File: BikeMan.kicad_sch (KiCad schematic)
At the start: 24 parts, among them J1 USB_A_stacked, J10 Conn_01x06_Male, J11 Conn_01x06_Male, J2 USB_A_stacked, J3 Barrel_Jack, J4 Conn_01x06_Female, J5 Conn_01x06_Female, J6 Conn_01x06_Female, J7 PushConnector_8pos, J8 PushConnector_8pos, J9 PushConnector_8pos, Q1 DMN62D0U-7, Q2 DMN62D0U-7

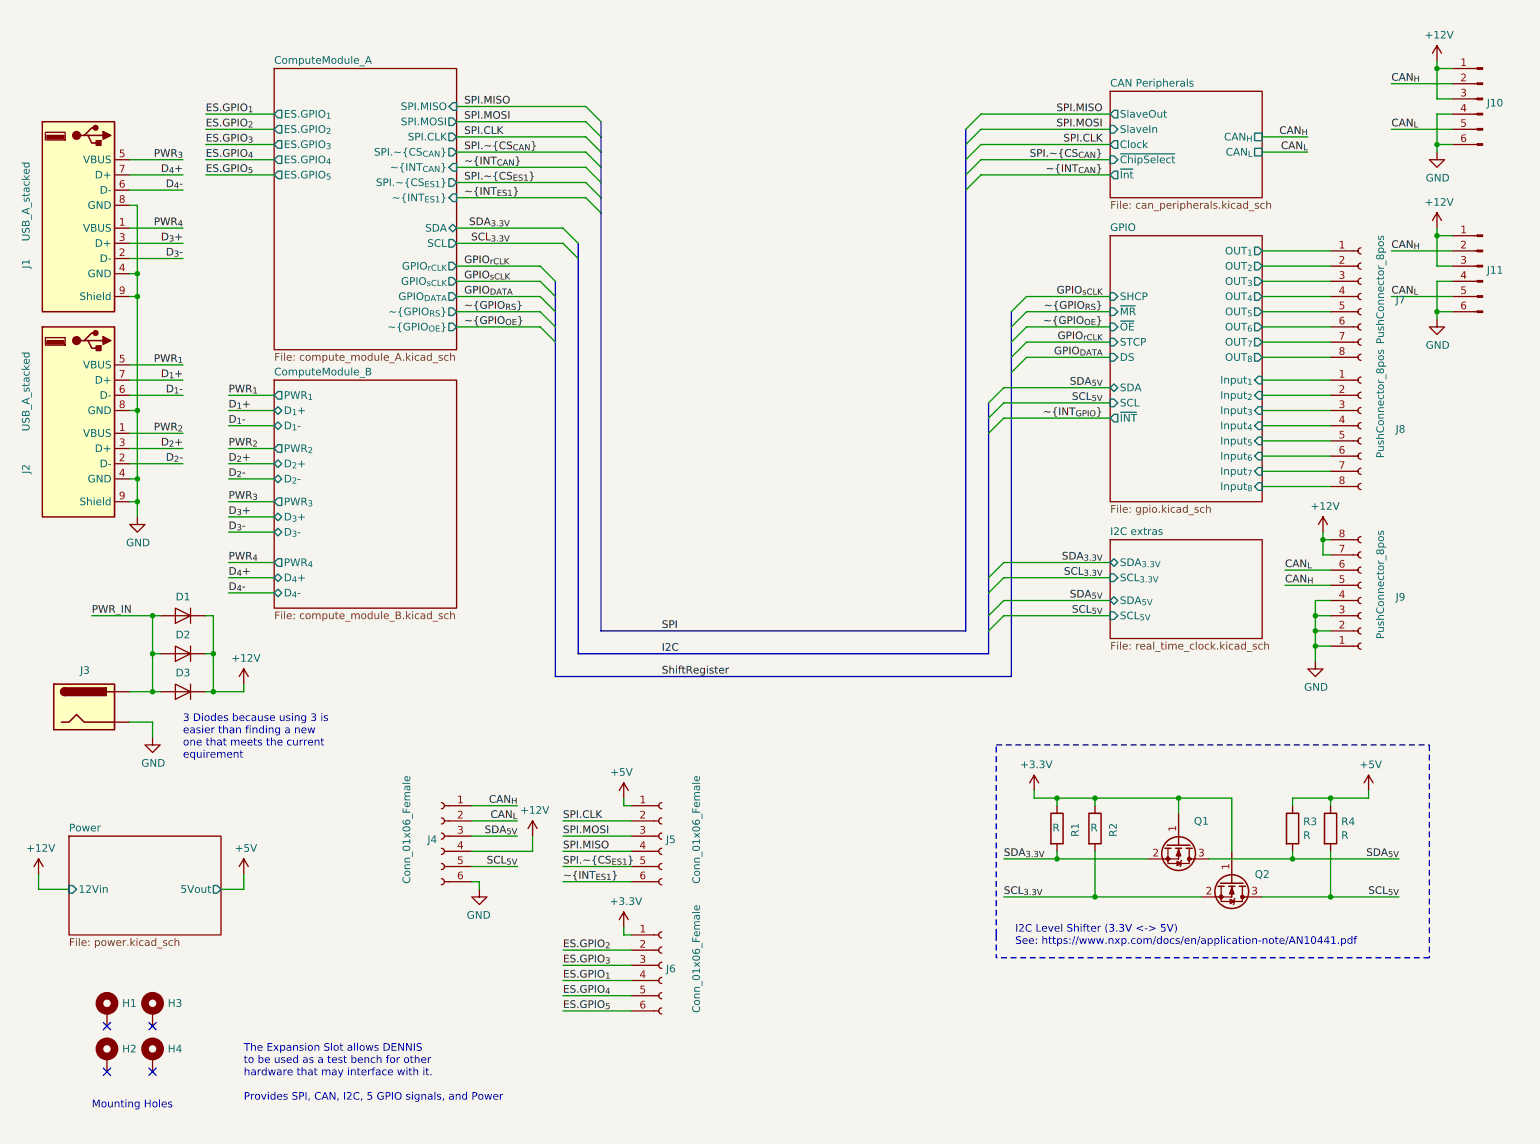
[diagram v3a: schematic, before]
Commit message: Cleaning up
Reassigned reference designators to better match their position on the board.
Moved USB hub IC and related circuits to their own sheet in the schematic.
Tweaked reference designator positions on board to improve visibility.
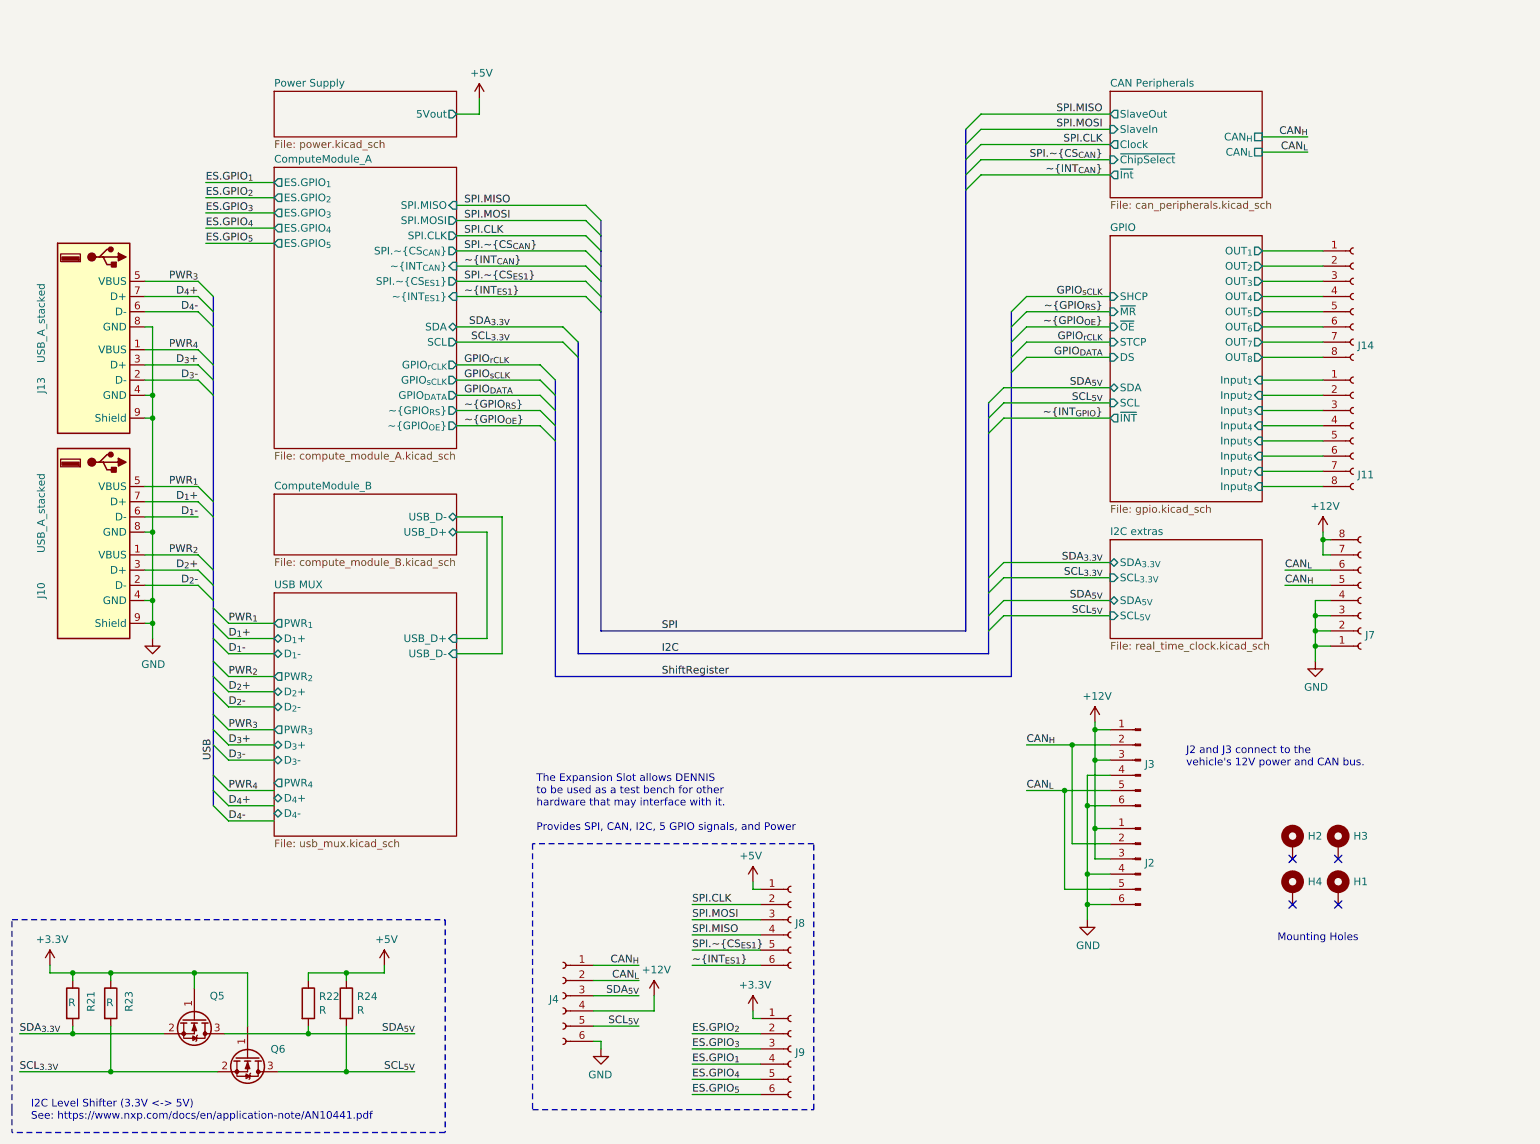
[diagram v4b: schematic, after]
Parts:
- removed D1, D2, D3: Diode, Diode_SMD:D_SOD-123F, symbol symbols:Diode
- removed J3: Barrel_Jack, Connector_BarrelJack:BarrelJack_Horizontal, symbol symbols:Barrel_Jack
- renumbered H4 to H1, H1 to H2, H2 to H4, J2 to J10, J8 to J11, J1 to J13, J7 to J14, J11 to J2, J10 to J3, J9 to J7, J5 to J8, J6 to J9, Q1 to Q5, Q2 to Q6, R1 to R21, R3 to R22, R2 to R23, R4 to R24
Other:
- sheet Power renamed Power Supply
- added sheet USB MUX (usb_mux.kicad_sch)
- sheet ComputeModule_B ports: added USB_D+, USB_D-; removed D_{1}+, D_{1}-, D_{2}+, D_{2}-, D_{3}+, D_{3}-, D_{4}+, D_{4}-, PWR_{1}, PWR_{2}, PWR_{3}, PWR_{4}
- sheet Power Supply ports: added none; removed 12Vin
- note added: "J2 and J3 connect to the vehicle's 12V power and CAN bus."
- note removed: "3 Diodes because using 3 is easier than finding a new one that meets the current equirement"
- moved on the sheet: H1, H2, H3, H4, J10, J11, J13, J14, J2, J3, J4, J8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

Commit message: migrated computers
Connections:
- net SPI.~CS_{ES1} renamed SPI.~{CS_{ES1}}
- net ~INT_{ES1} renamed ~{INT_{ES1}}
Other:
- sheet CAN Peripherals ports: added ~{ChipSelect}, ~{Int}; removed ~ChipSelect, ~Int
- sheet ComputeModule_A ports: added SPI.~{CS_{CAN}}, SPI.~{CS_{ES1}}, ~{GPIO_{OE}}, ~{GPIO_{RS}}, ~{INT_{CAN}}, ~{INT_{ES1}}; removed SPI.~CS_{CAN}, SPI.~CS_{ES1}, ~GPIO_{OE}, ~GPIO_{RS}, ~INT_{CAN}, ~INT_{ES1}
- sheet GPIO ports: added ~{INT}, ~{MR}, ~{OE}; removed ~INT, ~MR, ~OE

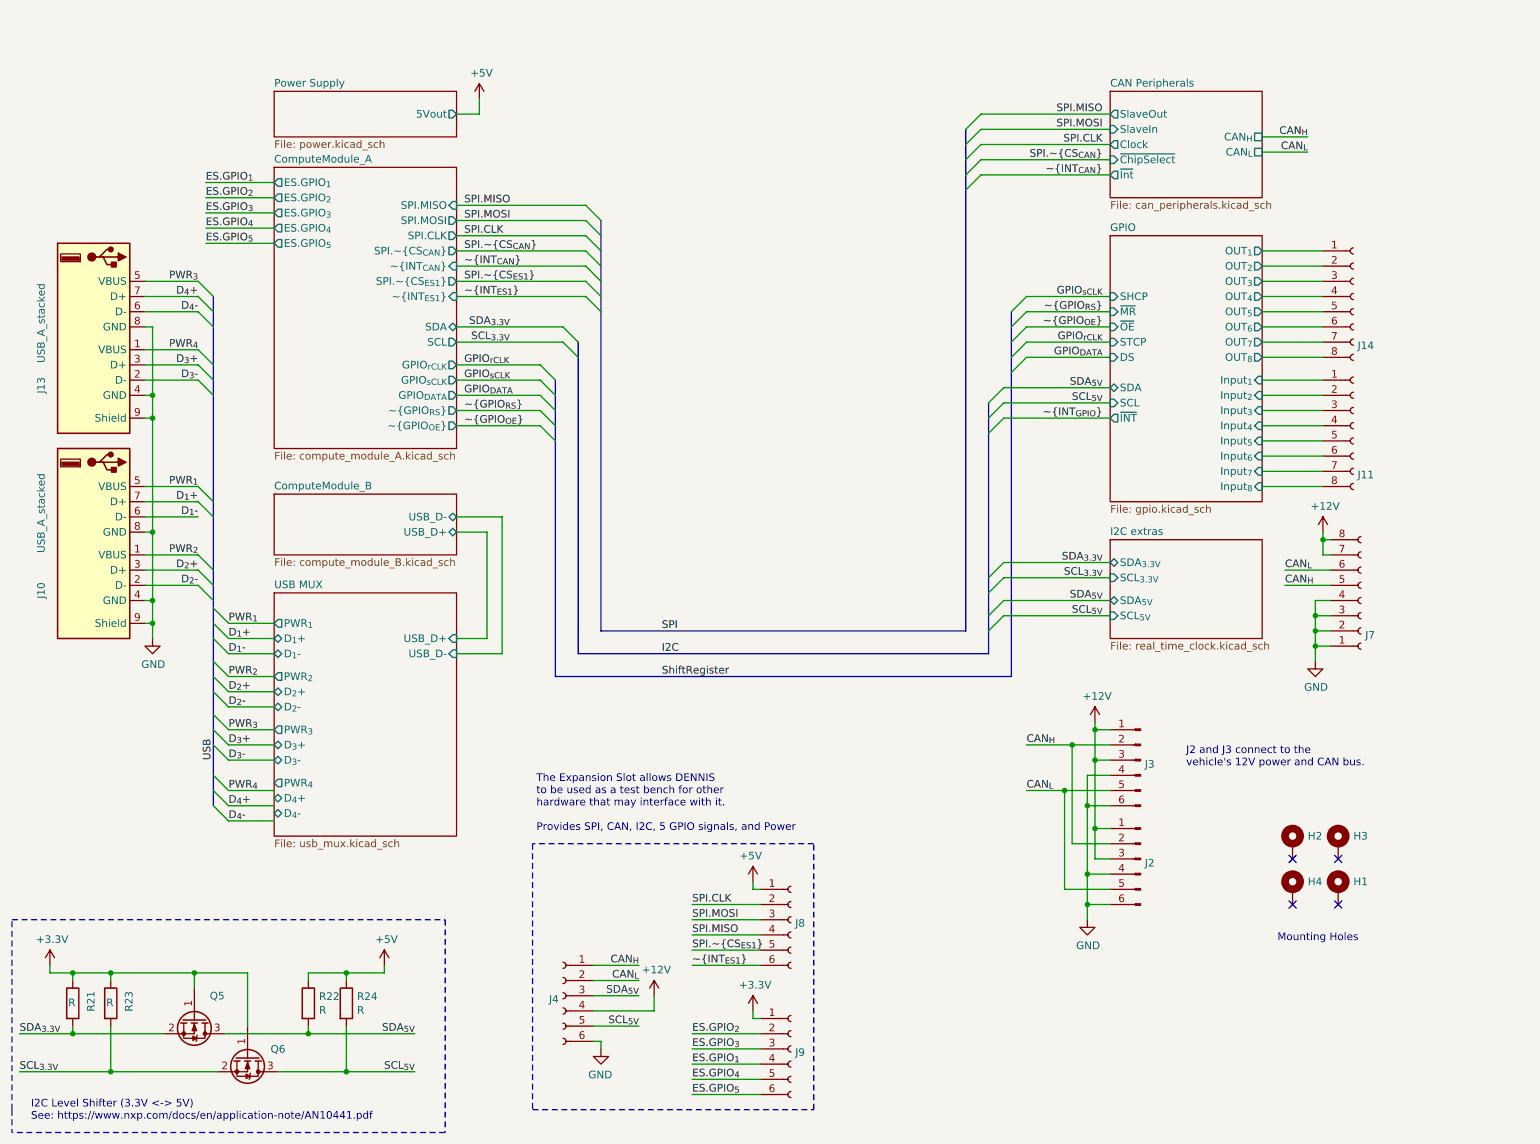
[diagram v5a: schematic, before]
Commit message: removed Compute Module
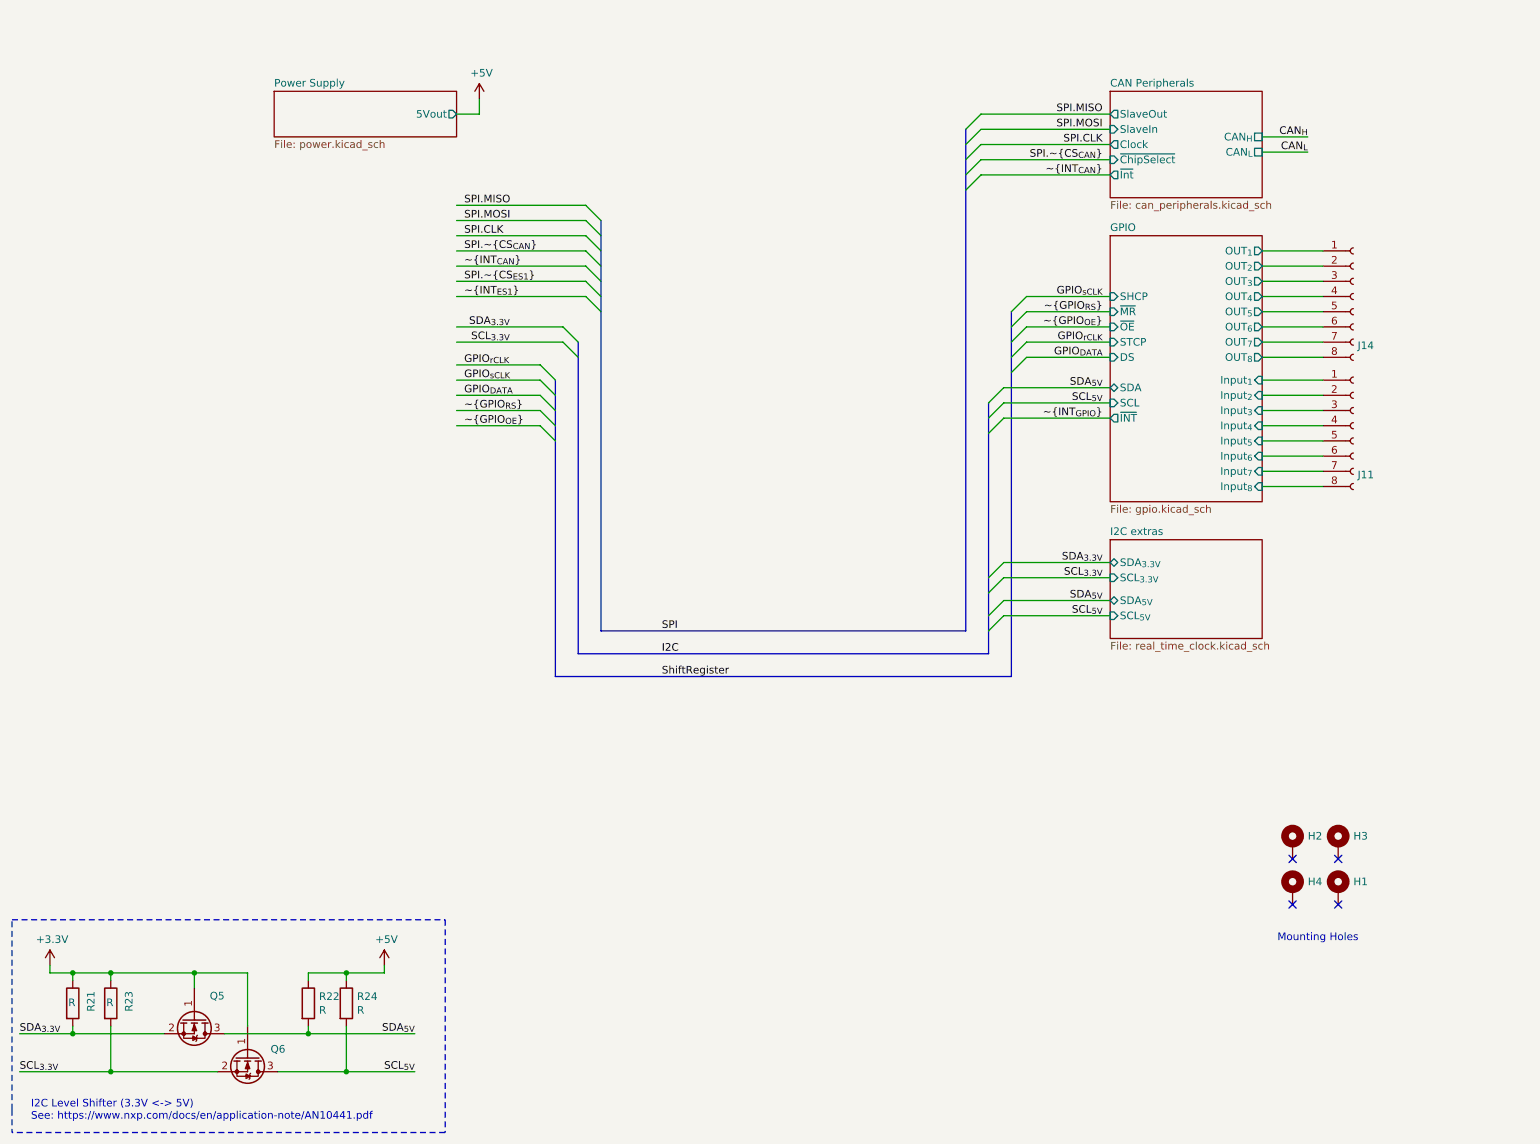
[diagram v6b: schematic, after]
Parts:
- removed J10, J13: USB_A_stacked, Connector_USB:USB_A_Wuerth_61400826021_Horizontal_Stacked, symbol symbols:USB_A_stacked
- removed J2, J3: Conn_01x06_Male, Connector_PinSocket_2.54mm:PinSocket_2x03_P2.54mm_Vertical, symbol Connector:Conn_01x06_Male
- removed J4, J8, J9: Conn_01x06_Female, Connector_PinSocket_2.54mm:PinSocket_2x03_P2.54mm_Vertical, symbol Connector:Conn_01x06_Female
- removed J7: PushConnector_8pos, footprints:CUI_TBL004-508-08BE-2BE, symbol symbols:PushConnector_8pos
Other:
- removed sheet ComputeModule_A
- removed sheet ComputeModule_B
- removed sheet USB MUX
- note removed: "J2 and J3 connect to the vehicle's 12V power and CAN bus."
- note removed: "The Expansion Slot allows DENNIS to be used as a test bench for other hardware that may interface with it. Provides SPI, CAN, I2C, 5 GPIO signals, and Power"

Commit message: layout sketching
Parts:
- added D5, D7: Diode, Diode_SMD:D_SOD-123F, symbol symbols:Diode
- added J3: Conn_01x06_Male, Connector_PinHeader_2.54mm:PinHeader_2x03_P2.54mm_Vertical, symbol Connector:Conn_01x06_Male
- added J4: MicroUSB, ecafe-racer:USB_Micro-B_Amphenol_10104110_Horizontal, symbol ecafe-racer:MicroUSB
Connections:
- net GPIO/Input_{7} is gone; now on net CAN_{L}: J11.7 (Pin_7)
- net GPIO/Input_{8} is gone; now on net CAN_{H}: J11.8 (Pin_8)
- net GPIO/OUT_{8} is gone; now on net GPIO/OUT_{7}: J14.8 (Pin_8)
- net +5V: now also J3.1 (Pin_1)
- net CAN_{H}: now also J3.2 (Pin_2)
- net CAN_{L}: now also J3.3 (Pin_3)
- net GPIO/OUT_{1}: now also J14.2 (Pin_2); no longer J14.1 (Pin_1)
- net GPIO/OUT_{2}: now also J14.3 (Pin_3); no longer J14.2 (Pin_2)
- net GPIO/OUT_{3}: now also J14.4 (Pin_4); no longer J14.3 (Pin_3)
- net GPIO/OUT_{4}: now also J14.5 (Pin_5); no longer J14.4 (Pin_4)
- net GPIO/OUT_{5}: now also J14.6 (Pin_6); no longer J14.5 (Pin_5)
- net GPIO/OUT_{6}: now also J14.7 (Pin_7); no longer J14.6 (Pin_6)
- net GPIO/OUT_{7}: no longer J14.7 (Pin_7)
- net GPIO/Input_{1} renamed BUS.PWR_{IN}
- net BUS.PWR_{IN}: now also D7.2 (A)
- net GPIO/Input_{2} renamed Input_{1}
- net GPIO/Input_{3} renamed Input_{2}
- net GPIO/Input_{4} renamed Input_{3}
- net GPIO/Input_{5} renamed Input_{4}
- net GPIO/Input_{6} renamed GND
- net GND: now also J3.6 (Pin_6)
- new net +12V: D5.2 (A), D7.1 (K)
- new net BUS.PWR_{OUT}: D5.1 (K), J14.1 (Pin_1)
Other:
- added sheet MicroController (micro_controller.kicad_sch)
- sheet GPIO ports: added none; removed Input_{5}, Input_{6}, Input_{7}, Input_{8}, OUT_{8}
- note added: "I2C Bus?"
- moved on the sheet: J11, J14
